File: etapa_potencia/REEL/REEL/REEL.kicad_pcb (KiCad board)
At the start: 2 copper layers, 93.2 x 73.9 mm, 47 parts, among them J1 Conn_display2, J2 Conn_display_2, J3 Conn_teclado, J4 Conn_audio, J5 USB_B_Mini, J6 Salida_amp, J7 Entrada_buzzer, SW1 SW_Push, SW3 SW_Push, SW4 BW, SW5 FW, U1 Tp5400, U2 ESP32-WROOM-32, U3 FT232, U4 AMS1117-3.3

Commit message: Nombres en capa silkscreen
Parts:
- renumbered SW4 to BW, J7 to Buzzer, J2 to Display, SW5 to FW, J3 to Keyboard, J5 to MicroUSB, SW3 to Prog, U3 to Programmer, SW1 to Reset, J1 to SDCard
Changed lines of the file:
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@@
     (property "Sheetname" "")
     (attr through_hole)
-    (fp_text reference "SW5" (at 2.13 -7.62) (layer "F.SilkS")
+    (fp_text reference "FW" (at 2.13 -7.62) (layer "F.SilkS")
       (effects (font (size 1 1) (thickness 0.15)))
     )
@@
     (property "Sheetname" "")
     (attr through_hole)
-    (fp_text reference "J1" (at 0 -2.33 90) (layer "F.SilkS")
+    (fp_text reference "SDCard" (at 2.54 7.65) (layer "F.SilkS")
       (effects (font (size 1 1) (thickness 0.15)))
     )
@@
     (property "Sheetname" "")
     (attr through_hole)
-    (fp_text reference "SW4" (at 9.75 0.245 90) (layer "F.SilkS")
+    (fp_text reference "BW" (at 9.75 0.245 90) (layer "F.SilkS")
       (effects (font (size 1 1) (thickness 0.15)))
     )
@@
     (property "Sheetname" "")
     (attr through_hole)
-    (fp_text reference "J2" (at 8.75 -2.8 90) (layer "F.SilkS")
+    (fp_text reference "Display" (at 8.75 -2.8 90) (layer "F.SilkS")
       (effects (font (size 1 1) (thickness 0.15)))
     )
@@
     (property "Sheetname" "")
     (attr through_hole)
-    (fp_text reference "J3" (at 6.858 3.81 90) (layer "F.SilkS")
+    (fp_text reference "Keyboard" (at 6.858 3.81 90) (layer "F.SilkS")
       (effects (font (size 1 1) (thickness 0.15)))
     )
@@
     (property "Sheetname" "")
     (attr smd)
-    (fp_text reference "SW3" (at 0.05 -4.445) (layer "F.SilkS")
+    (fp_text reference "Prog" (at 0.05 -4.445) (layer "F.SilkS")
       (effects (font (size 1 1) (thickness 0.15)))
     )
@@
     (property "Sheetname" "")
     (attr through_hole)
-    (fp_text reference "U3" (at -3.2 6.325 90) (layer "F.SilkS")
+    (fp_text reference "Programmer" (at -3.2 6.325 90) (layer "F.SilkS")
       (effects (font (size 1 1) (thickness 0.15)))
     )
@@
     (property "Sheetname" "")
     (attr through_hole)
-    (fp_text reference "J7" (at 1.25 -2.8 90) (layer "F.SilkS")
+    (fp_text reference "Buzzer" (at 1.25 -2.8 90) (layer "F.SilkS")
       (effects (font (size 1 1) (thickness 0.15)))
     )
@@
     (property "Sheetname" "Power")
     (attr smd)
-    (fp_text reference "J5" (at -3.625 -0.33 90) (layer "F.SilkS")
+    (fp_text reference "MicroUSB" (at -3.625 -0.33 90) (layer "F.SilkS")
       (effects (font (size 1 1) (thickness 0.15)))
     )
@@
     (property "Sheetname" "")
     (attr smd)
-    (fp_text reference "SW1" (at 0 -2.6 90) (layer "F.SilkS")
-      (effects (font (size 1 1) (thickness 0.15)))
-    )
+    (fp_text reference "Reset" (at 0 -2.6 90) (layer "F.SilkS")
+      (effects (font (size 1 1) (thickness 0.15)))
+    )

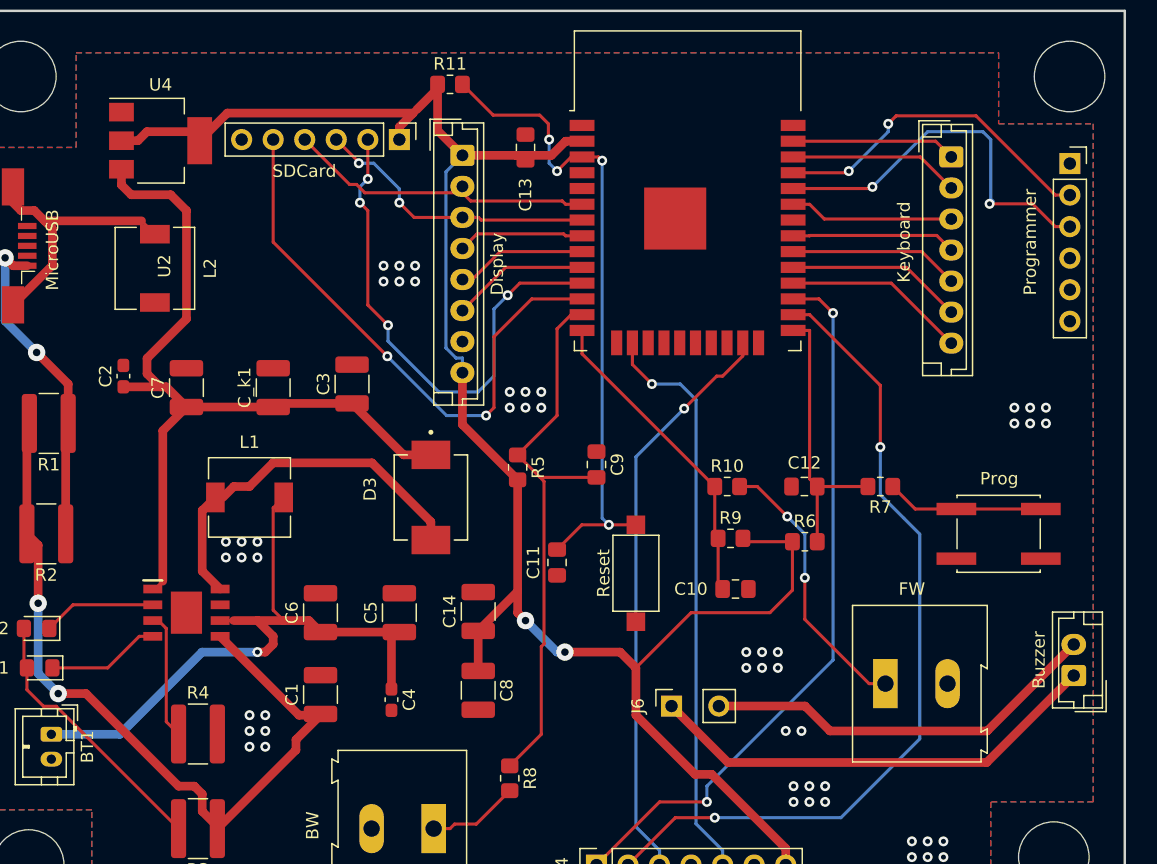
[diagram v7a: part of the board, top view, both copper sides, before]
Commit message: Últimos arreglos PCB
Resistencias de pull down de teclado y pin MISO de la sd, pin 12 queda libre, pines 34 y 35 quedan de entrada únicamente.
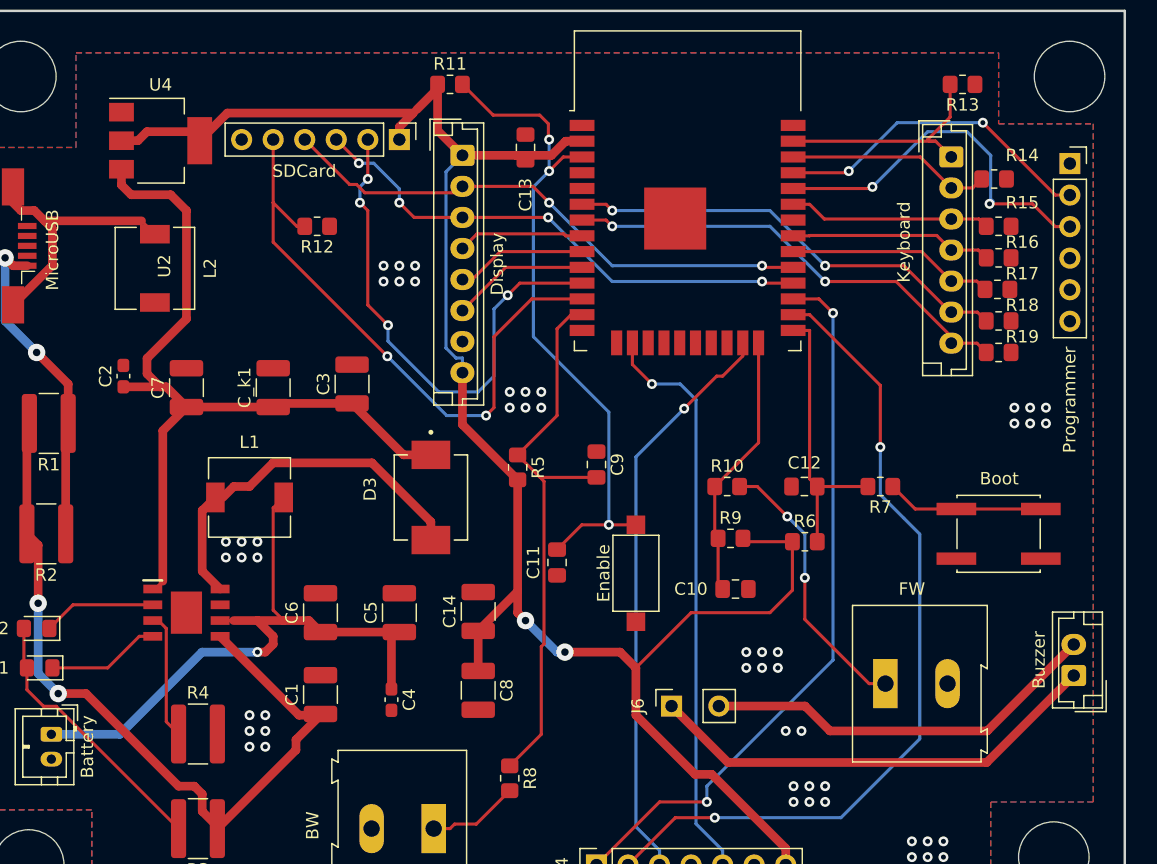
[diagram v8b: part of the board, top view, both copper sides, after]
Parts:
- added R12: 5.1k, Resistor_SMD:R_0805_2012Metric_Pad1.20x1.40mm_HandSolder, F.Cu at (63.9, 72.4)
- added R13: 5.1k, Resistor_SMD:R_0805_2012Metric_Pad1.20x1.40mm_HandSolder, F.Cu at (115.8, 61.0)
- added R14: 5.1k, Resistor_SMD:R_0805_2012Metric_Pad1.20x1.40mm_HandSolder, F.Cu at (118.4, 68.6)
- added R15: 5.1k, Resistor_SMD:R_0805_2012Metric_Pad1.20x1.40mm_HandSolder, F.Cu at (118.7, 72.4)
- added R16: 5.1k, Resistor_SMD:R_0805_2012Metric_Pad1.20x1.40mm_HandSolder, F.Cu at (118.7, 74.9)
- added R17: 5.1k, Resistor_SMD:R_0805_2012Metric_Pad1.20x1.40mm_HandSolder, F.Cu at (118.7, 77.5)
- added R18: 5.1k, Resistor_SMD:R_0805_2012Metric_Pad1.20x1.40mm_HandSolder, F.Cu at (118.7, 80.0)
- added R19: 5.1k, Resistor_SMD:R_0805_2012Metric_Pad1.20x1.40mm_HandSolder, F.Cu at (118.7, 82.5)
- renumbered BT1 to Battery, Prog to Boot, Reset to Enable
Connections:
- U2 pad 14: /FW -> unconnected-(U2-Pad14)
- U2 pad 24: unconnected-(U2-Pad24) -> /FW
- U2 pad 28: /T7 -> /MOSI
- U2 pad 29: /T6 -> /SCK
- U2 pad 6: /SCK -> /T6
- U2 pad 7: /MOSI -> /T7
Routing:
- net /T7: track 14.7 -> 37.3 mm, vias 0 -> 2
- net /T6: track 14.2 -> 36.4 mm, vias 0 -> 2
- net /SCK: track 25.0 -> 44.3 mm, vias 0 -> 2
- net /MOSI: track 23.2 -> 42.3 mm, vias 2 -> 4
- net /T1: track 13.3 -> 19.1 mm
- net /FW: track 25.5 -> 21.5 mm
- net /SDMISO: track 46.2 -> 49.5 mm
- net /T4: track 13.2 -> 16.3 mm
- net /T3: track 13.2 -> 16.3 mm
- net /T5: track 13.7 -> 16.7 mm
- net /T2: track 13.8 -> 16.5 mm
- net /TX_D0: track 27.2 -> 26.4 mm
- net /RX_D0: track 30.5 -> 29.8 mm
- net /EN: track 53.3 -> 53.9 mm, vias 4 -> 3
